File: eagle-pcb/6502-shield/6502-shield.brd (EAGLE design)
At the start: 101.6 x 53.3 mm, 28 parts, among them CON1 M20-7821646-FEM-HDR, SW1 MCSLPT4644B1TR-TACT-SW, SW2 PCM12SMTR-SPDT-RIGHT-ANG, U1 AT28C256TSOP-28, U13 74HC32TSSOP-14, U17 74HC04TSSOP-14, U2 W65C02S, U3 AS6C62256, U4 W65C22, U5 MM74HC00TSSOP, U6 SE555QS, U7 SE555QS, U8 SE555QS

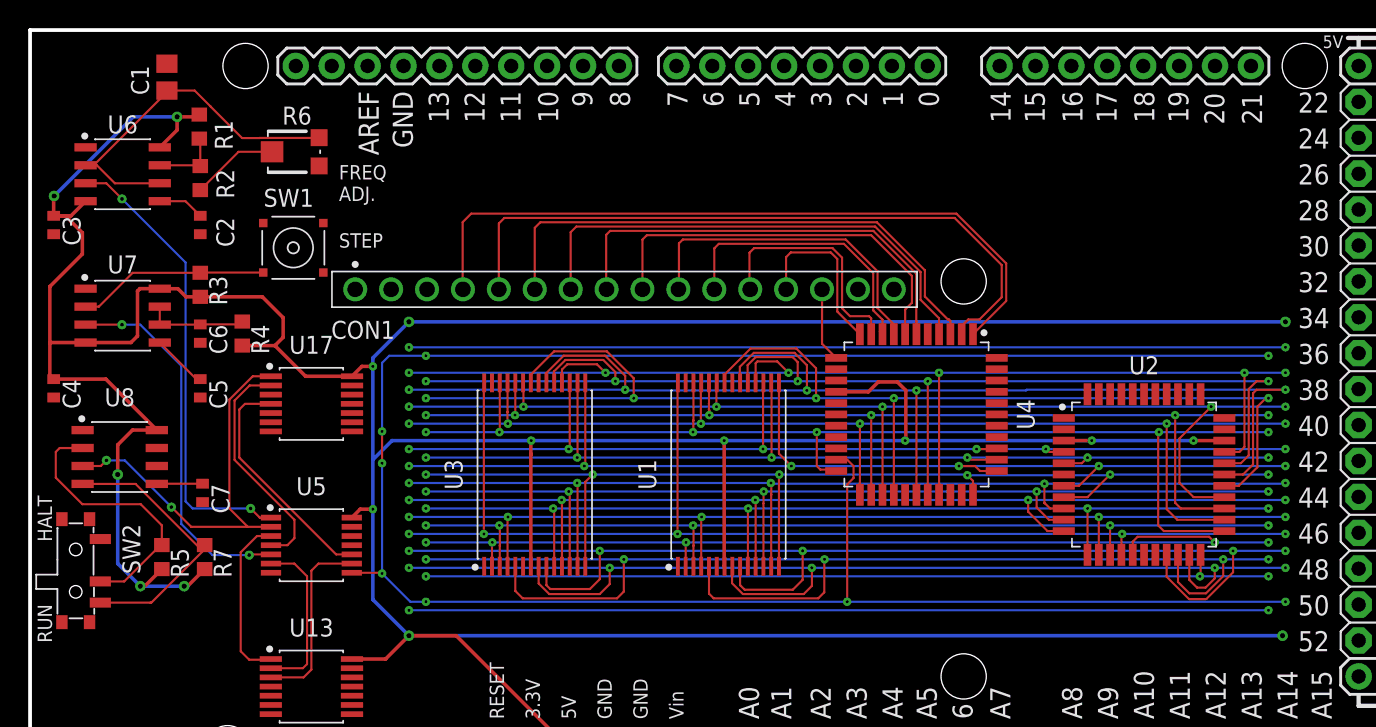
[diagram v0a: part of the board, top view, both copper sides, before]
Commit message: added lattice machx02-256 FPGA in tqfp100 package - symbol, footprint, 3d model
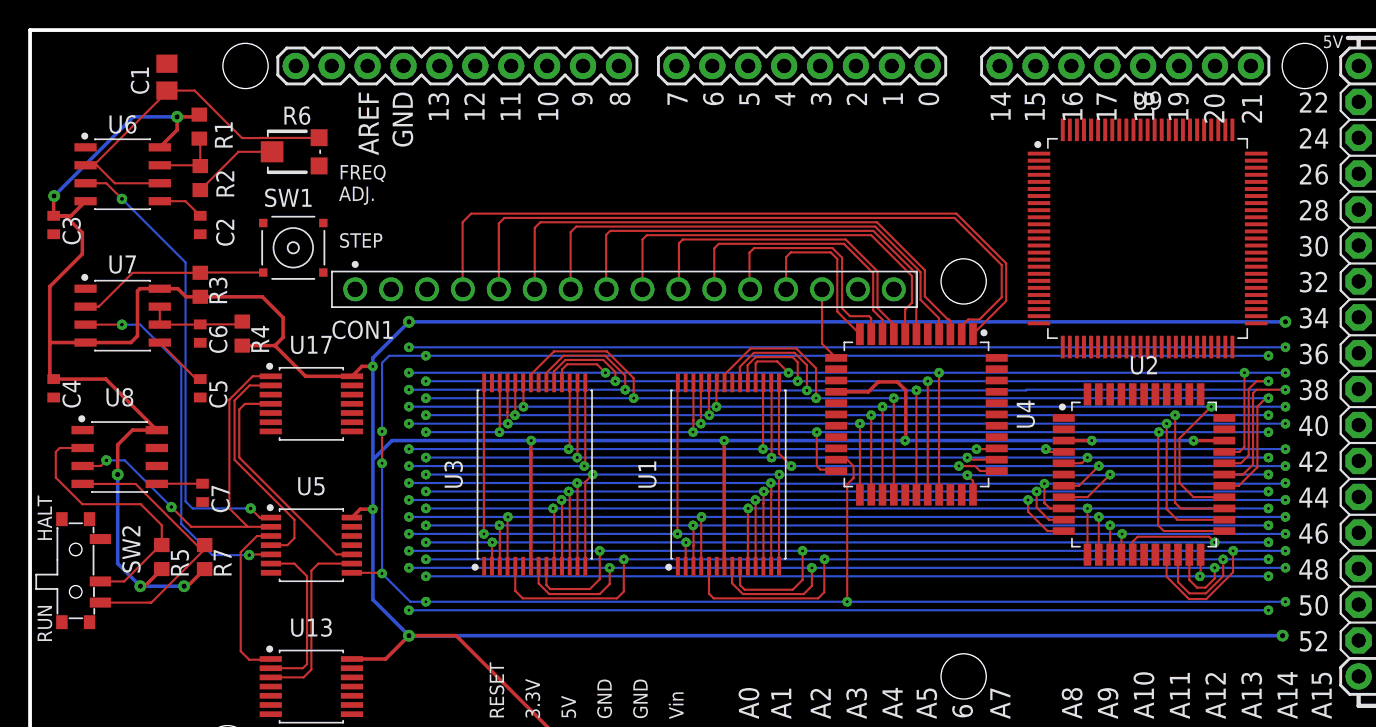
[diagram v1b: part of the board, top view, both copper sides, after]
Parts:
- added U9: MACHXO-FPGA100TQFP, 6502-shield:QFP50P1600X1600X160-100N
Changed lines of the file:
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@@
 </layers>
 <board>
-<fusionsync huburn="a.YnVzaW5lc3M6Z21haWw3MDQ2MzI" projecturn="a.YnVzaW5lc3M6Z21haWw3MDQ2MzIjMjAyMDAzMjMyNzc5NDAzNTE" f3durn="urn:adsk.wipprod:dm.lineage:SKI6Y7I3R2GK5LyZdhPrew" pcbguid="6684de3e-4798-432d-a463-1731bf560a7c" lastpulledtime="2020-03-23T21:54:50Z" lastsyncedchangeguid="26928c01-5e82-ac68-2b74-82bd82c14e25" latestrevisionid="" lastsyncedrevisionid="" lastboardhashguid="bb699a26-ff62-3385-8bdc-24f4424fb3f4" lastpushedtime="2020-03-30T21:33:14Z" linktopcb3d="%12"/>
+<fusionsync huburn="a.YnVzaW5lc3M6Z21haWw3MDQ2MzI" projecturn="a.YnVzaW5lc3M6Z21haWw3MDQ2MzIjMjAyMDAzMjMyNzc5NDAzNTE" f3durn="urn:adsk.wipprod:dm.lineage:SKI6Y7I3R2GK5LyZdhPrew" pcbguid="6684de3e-4798-432d-a463-1731bf560a7c" lastpulledtime="2020-03-23T21:54:50Z" lastsyncedchangeguid="26928c01-5e82-ac68-2b74-82bd82c14e25" latestrevisionid="" lastsyncedrevisionid="" lastboardhashguid="746e7fcb-8667-d4be-1ace-f9509a1cfff9" lastpushedtime="2020-04-02T16:11:19Z" linktopcb3d="%12"/>
 <plain>
 <wire x1="0" y1="0" x2="99.06" y2="0" width="0.254" layer="20"/>
@@
 </class>
 </classes>
-<designrules name="default">
-<description language="de">&lt;b&gt;EAGLE Design Rules&lt;/b&gt;
-&lt;p&gt;
-Die Standard-Design-Rules sind so gewählt, dass sie für
-die meisten Anwendungen passen. Sollte ihre Platine
-besondere Anforderungen haben, treffen Sie die erforderlichen
-Einstellungen hier und speichern die Design Rules unter
-einem neuen Namen ab.</description>
+<designrules name="SparkFun">
 <description language="en">&lt;b&gt;EAGLE Design Rules&lt;/b&gt;
 &lt;p&gt;
@@
 <param name="mtCopper" value="0.035mm 0.035mm 0.035mm 0.035mm 0.035mm 0.035mm 0.035mm 0.035mm 0.035mm 0.035mm 0.035mm 0.035mm 0.035mm 0.035mm 0.035mm 0.035mm"/>
 <param name="mtIsolate" value="1.5mm 0.15mm 0.2mm 0.15mm 0.2mm 0.15mm 0.2mm 0.15mm 0.2mm 0.15mm 0.2mm 0.15mm 0.2mm 0.15mm 0.2mm"/>
-<param name="mdWireWire" value="6mil"/>
-<param name="mdWirePad" value="6mil"/>
-<param name="mdWireVia" value="6mil"/>
-<param name="mdPadPad" value="6mil"/>
-<param name="mdPadVia" value="6mil"/>
-<param name="mdViaVia" value="6mil"/>
-<param name="mdSmdPad" value="6mil"/>
-<param name="mdSmdVia" value="6mil"/>
-<param name="mdSmdSmd" value="6mil"/>
-<param name="mdViaViaSameLayer" value="6mil"/>
+<param name="mdWireWire" value="8mil"/>
+<param name="mdWirePad" value="8mil"/>
+<param name="mdWireVia" value="8mil"/>
+<param name="mdPadPad" value="8mil"/>
+<param name="mdPadVia" value="8mil"/>
+<param name="mdViaVia" value="8mil"/>
+<param name="mdSmdPad" value="8mil"/>
+<param name="mdSmdVia" value="8mil"/>
+<param name="mdSmdSmd" value="8mil"/>
+<param name="mdViaViaSameLayer" value="8mil"/>
 <param name="mnLayersViaInSmd" value="2"/>
-<param name="mdCopperDimension" value="40mil"/>
-<param name="mdDrill" value="6mil"/>
+<param name="mdCopperDimension" value="8mil"/>
+<param name="mdDrill" value="8mil"/>
 <param name="mdSmdStop" value="0mil"/>
-<param name="msWidth" value="6mil"/>
-<param name="msDrill" value="0.35mm"/>
+<param name="msWidth" value="8mil"/>
+<param name="msDrill" value="20mil"/>
 <param name="msMicroVia" value="9.99mm"/>
 <param name="msBlindViaRatio" value="0.5"/>
@@
 <param name="rvMicroViaOuter" value="0.25"/>
 <param name="rvMicroViaInner" value="0.25"/>
-<param name="rlMinPadTop" value="10mil"/>
+<param name="rlMinPadTop" value="12mil"/>
 <param name="rlMaxPadTop" value="20mil"/>
 <param name="rlMinPadInner" value="10mil"/>
 <param name="rlMaxPadInner" value="20mil"/>
-<param name="rlMinPadBottom" value="10mil"/>
+<param name="rlMinPadBottom" value="12mil"/>
 <param name="rlMaxPadBottom" value="20mil"/>
-<param name="rlMinViaOuter" value="8mil"/>
+<param name="rlMinViaOuter" value="10mil"/>
 <param name="rlMaxViaOuter" value="20mil"/>
-<param name="rlMinViaInner" value="8mil"/>
+<param name="rlMinViaInner" value="10mil"/>
 <param name="rlMaxViaInner" value="20mil"/>
 <param name="rlMinMicroViaOuter" value="4mil"/>
@@
 <param name="mlMinCreamFrame" value="0mil"/>
 <param name="mlMaxCreamFrame" value="0mil"/>
-<param name="mlViaStopLimit" value="0mil"/>
+<param name="mlViaStopLimit" value="20mil"/>
 <param name="srRoundness" value="0"/>
 <param name="srMinRoundness" value="0mil"/>
@@
 <attribute name="VALUE" x="23" y="33.105" size="1.27" layer="27" align="top-center"/>
 </element>
+<element name="U9" library="6502-shield" library_urn="urn:adsk.eagle:library:18477216" package="QFP50P1600X1600X160-100N" package3d_urn="urn:adsk.eagle:package:18828921/1" value="MACHXO-FPGA100TQFP" x="79.05" y="38.6" smashed="yes">
+<attribute name="NAME" x="79.05" y="47.7162" size="1.27" layer="25" align="bottom-center"/>
+<attribute name="VALUE" x="79.05" y="29.4838" size="1.27" layer="27" align="top-center"/>
+</element>
 </elements>

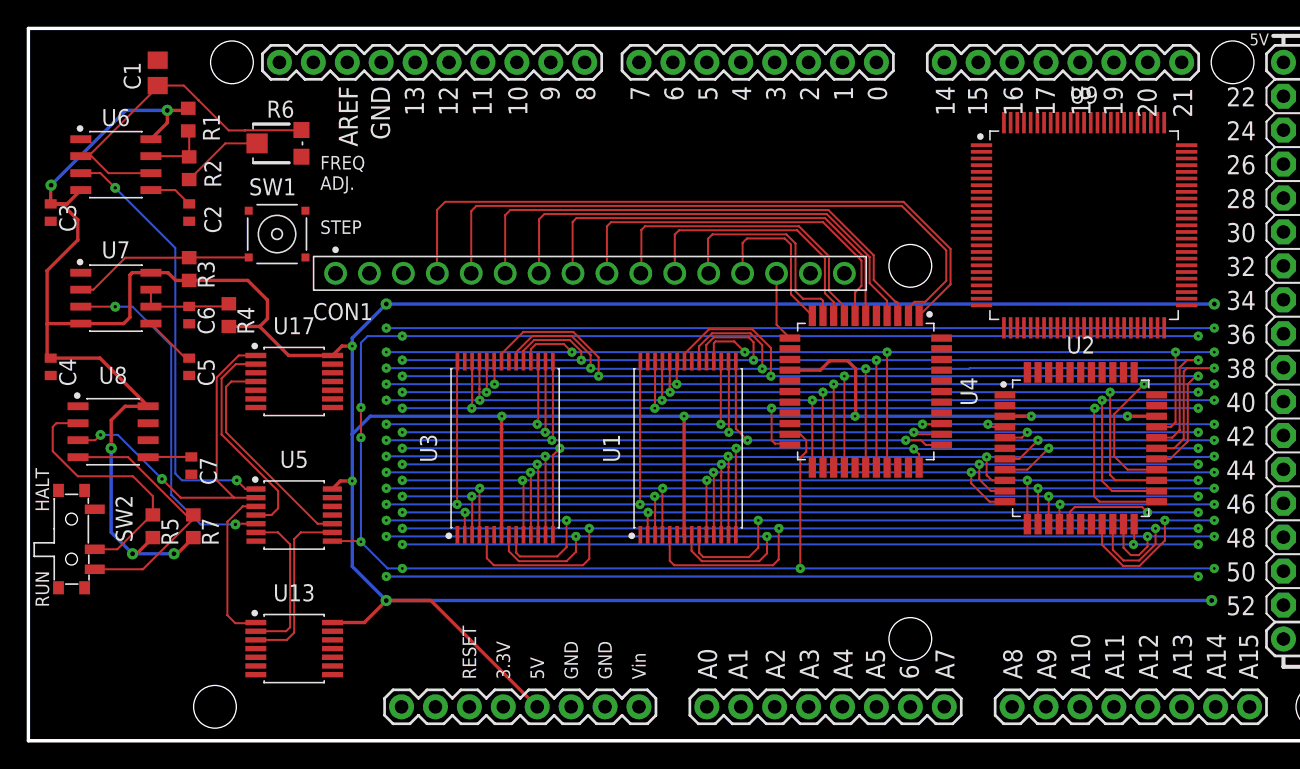
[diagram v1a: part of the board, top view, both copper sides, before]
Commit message: got the fpga based design done (first pass).  Notional parts placement, no routing.
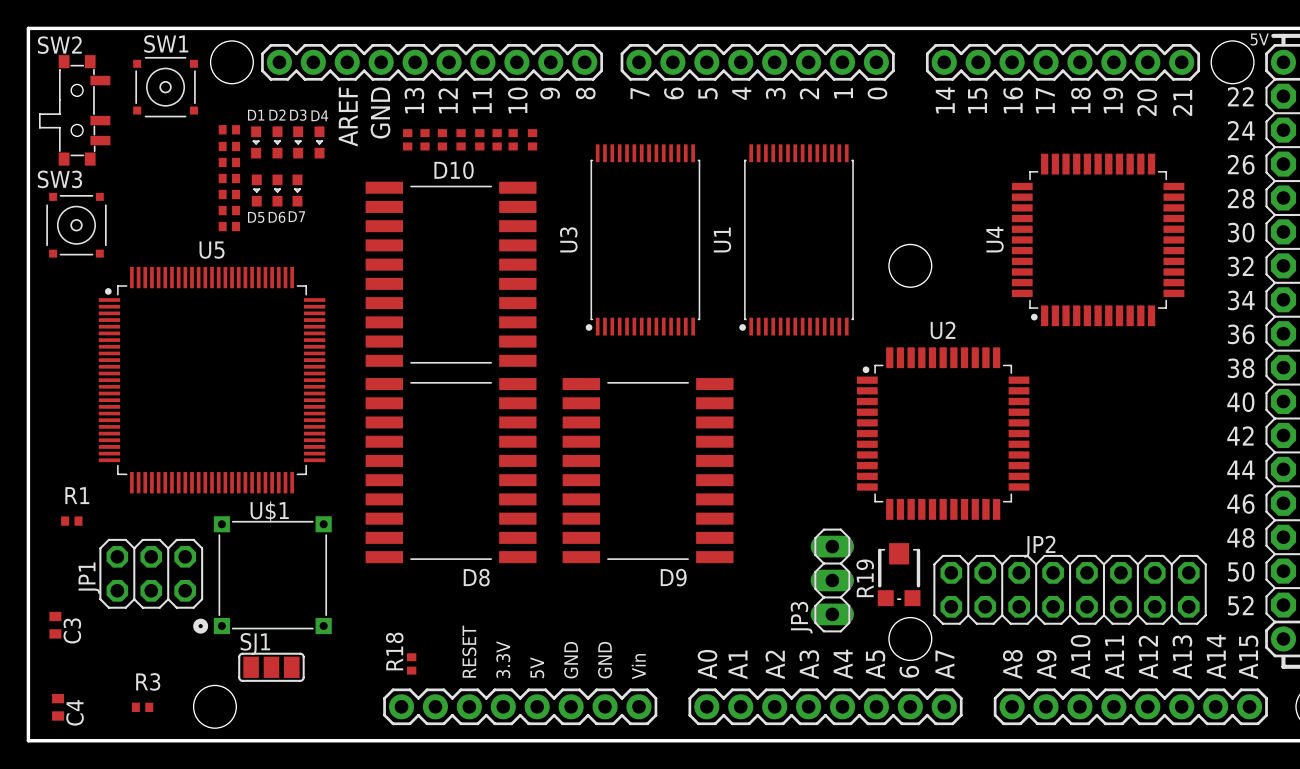
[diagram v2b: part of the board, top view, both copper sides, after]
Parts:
- removed C1: 1uF, rcl:C0805
- removed C2, C5, C7: 0.01uF, rcl:C0402
- removed C6: 0.1uF, rcl:C0402
- removed CON1: M20-7821646-FEM-HDR, 6502-shield:HDRVR16W64P254_1X16_4104X250X865B
- removed U13: 74HC32TSSOP-14, 6502-shield:SOP65P640X110-14N
- removed U17: 74HC04TSSOP-14, 6502-shield:SOP65P640X110-14N
- removed U6, U7, U8: SE555QS, 6502-shield:SOIC127P600X150-8N
- removed U9: MACHXO-FPGA100TQFP, 6502-shield:QFP50P1600X1600X160-100N
- added D1, D2, D3, D4, D5, D6, D7: (no value), we-led:WL-SMCD_0603
- added D10, D8, D9: ACDC02-41SGWA-DUAL-7SEG, 6502-shield:ACDC02-41S-DUAL-7SEG
- added JP1: (no value), pinhead:2X03
- added JP2: (no value), pinhead:2X08
- added JP3: (no value), pinhead:1X03
- added R10, R11, R12, R13, R14, R15, R16, R17: 330, rcl:R0402
- added R18: 10K, rcl:R0402
- added R19: 10K, 6502-shield:TC33X
- added R8, R9: 390, rcl:R0402
- added SJ1: (no value), jumper:SJ_2
- added SW3: MCSLPT4644B1TR-TACT-SW, 6502-shield:MCSLPT4644B1TR-TACT-SW
- added U$1: CRYSTAL-OSC-DIP8/4, 6502-shield:DIP8/4
- R1: value 1K -> 10K; device rcl:R0603 -> rcl:R0402
- R2, R5, R7: value 1K -> 390; device rcl:R0603 -> rcl:R0402
- R3: value 1K -> 4.7K; device rcl:R0603 -> rcl:R0402
- R4: value 1M -> 390; device rcl:R0603 -> rcl:R0402
- R6: value 1M -> 390; device 6502-shield:TC33X -> rcl:R0402
- U5: value MM74HC00TSSOP -> MACHXO-FPGA100TQFP; device 6502-shield:SOP65P635X120-14N -> 6502-shield:QFP50P1600X1600X160-100N
- moved R3 33.0 mm to (8.55, 2.50), turned to 0 degrees
- moved SW2 32.1 mm to (3.65, 47.2)
- moved R1 31.3 mm to (3.25, 16.4), turned to 0 degrees
- moved C3 30.9 mm to (2.02, 8.65)
- moved C4 25.5 mm to (2.22, 2.50)
- moved R7 25.0 mm to (15.1, 40.9), turned to 0 degrees
- moved R5 24.3 mm to (15.1, 39.7), turned to 0 degrees
- moved U4 20.8 mm to (80.1, 37.5), turned to 90 degrees
- moved U3 18.8 mm to (46.2, 37.5)
- moved U1 17.7 mm to (57.7, 37.5)
- moved SW1 13.8 mm to (10.3, 48.9)
- moved U5 11.8 mm to (13.8, 27.0)
- moved R4 11.4 mm to (15.1, 43.3), turned to 0 degrees
- moved U2 10.4 mm to (68.5, 23.0)
- moved R2 5.31 mm to (15.1, 38.5), turned to 0 degrees
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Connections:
- removed net CLK_0: U5.1, U6.3
- removed net CLK_1: U5.5, U7.3
- removed net CLK_HALT: U17.3
- removed net CLK_SELECT: U17.1, U5.2, U8.3
- removed net TRIG: C1.1, R6.3, U6.2, U6.6
- new net BE: U2.34, U5.38
- new net CLK_SEL: SJ1.2, U5.18
- new net DIGIT1_EN: D8.18, D8.3, U5.87
- new net DIGIT2_EN: D8.13, D8.8, U5.89
- new net DIGIT3_EN: D9.18, D9.3, U5.91
- new net DIGIT4_EN: D9.13, D9.8, U5.94
- new net DIGIT5_EN: D10.18, D10.3, U5.95
- new net DIGIT6_EN: D10.13, D10.8, U5.96
- new net DIGIT_A: R10.2, U5.78
- new net DIGIT_B: R11.2, U5.79
- new net DIGIT_C: R12.2, U5.80
- new net DIGIT_D: R13.2, U5.81
- new net DIGIT_DP: R17.2, U5.86
- new net DIGIT_E: R14.2, U5.82
- new net DIGIT_F: R15.2, U5.83
- new net DIGIT_G: R16.2, U5.85
- new net DMA: PCB1.47, U5.32
- new net IO_EN: U4.19, U5.36
- new net IRQN: U2.43, U4.17, U5.44
- new net N$15: D4.1, R9.2
- new net N$16: D4.2, U5.100
- new net N$17: D7.2, U5.99
- new net N$18: D3.2, U5.98
- new net N$19: D6.2, U5.97
- new net N$20: D1.1, R4.1
- new net N$21: D2.1, R2.1
- new net N$22: D5.1, R5.1
- new net N$23: D10.12, D10.17, D8.12, D8.17, D9.12, D9.17, R10.1
- new net N$24: D10.11, D10.16, D8.11, D8.16, D9.11, D9.16, R11.1
- new net N$25: D10.4, D10.9, D8.4, D8.9, D9.4, D9.9, R12.1
- new net N$26: D10.2, D10.7, D8.2, D8.7, D9.2, D9.7, R13.1
- new net N$27: D10.1, D10.6, D8.1, D8.6, D9.1, D9.6, R14.1
- new net N$28: D10.14, D10.19, D8.14, D8.19, D9.14, D9.19, R15.1
- new net N$29: D10.15, D10.20, D8.15, D8.20, D9.15, D9.20, R16.1
- new net N$30: D10.10, D10.5, D8.10, D8.5, D9.10, D9.5, R17.1
- new net N$31: R18.1, U2.41
- new net N$32: JP3.2, R19.2
- new net N$34: U$1.5, U5.17
- new net OE: PCB1.39, U1.1, U3.1, U5.73
- new net RAM_EN: U3.27, U5.76
- new net RESETN: U2.38, U4.31, U5.39
- new net ROM_EN: U1.27, U5.77
- new net ROM_PGM: PCB1.45, U5.34
- new net RW: U2.32, U4.18, U5.43
- new net WE: PCB1.41, U1.6, U3.6, U5.72
- net A0: now also PCB1.22, U5.54
- net A1: now also PCB1.24, U5.55
- net A10: now also PCB1.42, U5.66
- net A11: now also PCB1.44, U5.67
- net A12: now also PCB1.46, U5.68
- net A13: now also PCB1.48, U5.69
- net A14: now also PCB1.50, U5.70
- net A15: now also PCB1.52, U5.71
- net A2: now also PCB1.26, U5.56
- net A3: now also PCB1.28, U5.57
- net A4: now also PCB1.30, U5.58
- net A5: now also PCB1.32, U5.59
- net A6: now also PCB1.34, U5.61
- net A7: now also PCB1.36, U5.63
- net A8: now also PCB1.38, U5.64
- net A9: now also PCB1.40, U5.65
- net CLK: now also PCB1.43, U2.35, U5.37; no longer U5.8
- net D0: now also PCB1.23, U5.45
- net D1: now also PCB1.25, U5.46
- net D2: now also PCB1.27, U5.47
- net D3: now also PCB1.29, U5.49
- net D4: now also PCB1.31, U5.50
- net D5: now also PCB1.33, U5.51
- net D6: now also PCB1.35, U5.52
- net D7: now also PCB1.37, U5.53
- net GND: now also JP1.5, JP3.3, R19.1, R2.2, R3.1, R4.2, R5.2, R6.1, R7.1, R8.1, R9.1, SJ1.3, SW2.3, SW3.T2, U$1.4, U5.12, U5.25, U5.40, U5.42, U5.62, U5.75, U5.84, U5.93; no longer C1.2, C2.2, C5.2, C6.2, C7.2, SW2.1, U13.7, U17.7, U2.17, U2.18, U2.39, U5.7, U6.1, U7.1, U8.1, U8.6
- net N$1: now also R1.1, U5.48; no longer R2.2, R6.2
- net N$10: now also D2.2, U5.2; no longer U17.2, U5.4
- net N$11: now also D5.2; no longer U13.1
- net N$12: now also D6.1, R6.2; no longer U13.2, U5.6
- net N$13: now also D3.1, R7.2; no longer U13.3, U5.9
- net N$14: now also D7.1, R8.2; no longer U17.4, U5.10
- net N$2: now also SW3.T4, U5.5; no longer C2.1, U6.5
- net N$3: now also SW1.T4, U5.14; no longer R1.1, R2.1, U6.7
- net N$4: now also JP1.2, U5.31; no longer R3.1, SW1.T3, U7.2
- net N$5: now also JP1.3, U5.26; no longer C5.1, U7.5
- net N$6: now also JP1.4, U5.33; no longer C6.1, R4.1, U7.6, U7.7
- net N$7: now also JP1.6, R3.2, U5.28; no longer R5.1, SW2.2, U8.2
- net N$8: now also SW2.1, U5.4; no longer R7.1, SW2.3, U8.4
- net N$9: now also D1.2, U5.1; no longer C7.1, U8.5
- net PA0: now also JP2.1
- net PA1: now also JP2.3
- net PA2: now also JP2.5
- net PA3: now also JP2.7
- net PA4: now also JP2.9
- net PA5: now also JP2.11; no longer CON1.4
- net PA6: now also JP2.13; no longer CON1.5
- net PA7: now also JP2.15; no longer CON1.6
- net PB0: now also JP2.2; no longer CON1.7
- net PB1: now also JP2.4; no longer CON1.8
- net PB2: now also JP2.6; no longer CON1.9
- net PB3: now also JP2.8; no longer CON1.10
- net PB4: now also JP2.10; no longer CON1.11
- net PB5: now also JP2.12; no longer CON1.12
- net PB6: now also JP2.14; no longer CON1.13
- net PB7: now also JP2.16; no longer CON1.14
- net VCC: now also JP1.1, JP3.1, PCB1.3.3V, R18.2, U$1.8, U2.1, U4.20, U5.10, U5.24, U5.35, U5.41, U5.60, U5.74, U5.88, U5.90, U5.92; no longer PCB1.5V, PCB1.5V., PCB1.5V.., R3.2, R4.2, R5.2, R7.2, U13.14, U17.14, U5.14, U6.4, U6.8, U7.4, U7.8, U8.8
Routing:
- net VCC: track 355.3 -> 0.00 mm, vias 16 -> 0
- net CLK: track 155.9 -> 0.00 mm, vias 8 -> 0
- net CLK_N: track 122.8 -> 0.00 mm, vias 4 -> 0
- net D2: track 96.0 -> 0.00 mm, vias 5 -> 0
- net D3: track 95.9 -> 0.00 mm, vias 5 -> 0
- net A13: track 91.6 -> 0.00 mm, vias 5 -> 0
- net D1: track 88.9 -> 0.00 mm, vias 5 -> 0
- net A12: track 87.0 -> 0.00 mm, vias 5 -> 0
- net D0: track 86.0 -> 0.00 mm, vias 6 -> 0
- net A10: track 84.9 -> 0.00 mm, vias 5 -> 0
- net A14: track 83.5 -> 0.00 mm, vias 5 -> 0
- net D6: track 83.3 -> 0.00 mm, vias 6 -> 0
- net D7: track 82.0 -> 0.00 mm, vias 6 -> 0
- net D4: track 81.5 -> 0.00 mm, vias 6 -> 0
- net A2: track 80.1 -> 0.00 mm, vias 6 -> 0
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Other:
- board text removed: "FREQ ADJ."
- board text removed: "HALT"
- board text removed: "RUN"
- board text removed: "STEP"
